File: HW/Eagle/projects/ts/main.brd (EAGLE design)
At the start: 80 x 45 mm, 47 parts, among them IC1 4050D, Q1 20 MHz, T1 IRFZ24N, T2 IRFZ24N, U1 ATMEGA328P-PU, U2 LM2576T, U3 HT7533, U4 LM75

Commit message: Replaced R1 due to improper LCD reset procedure
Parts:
- R1: value 10k -> 1M
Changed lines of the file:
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@@
 <attribute name="VALUE" x="42.21" y="16.27" size="1.27" layer="27" rot="R270"/>
 </element>
-<element name="R1" library="rcl" package="R0805" value="10k" x="58.5" y="41.5" smashed="yes">
+<element name="R1" library="rcl" package="R0805" value="1M" x="58.5" y="41.5" smashed="yes">
 <attribute name="NAME" x="60.865" y="41.27" size="1.27" layer="25"/>
 <attribute name="VALUE" x="57.865" y="38.96" size="1.27" layer="27"/>

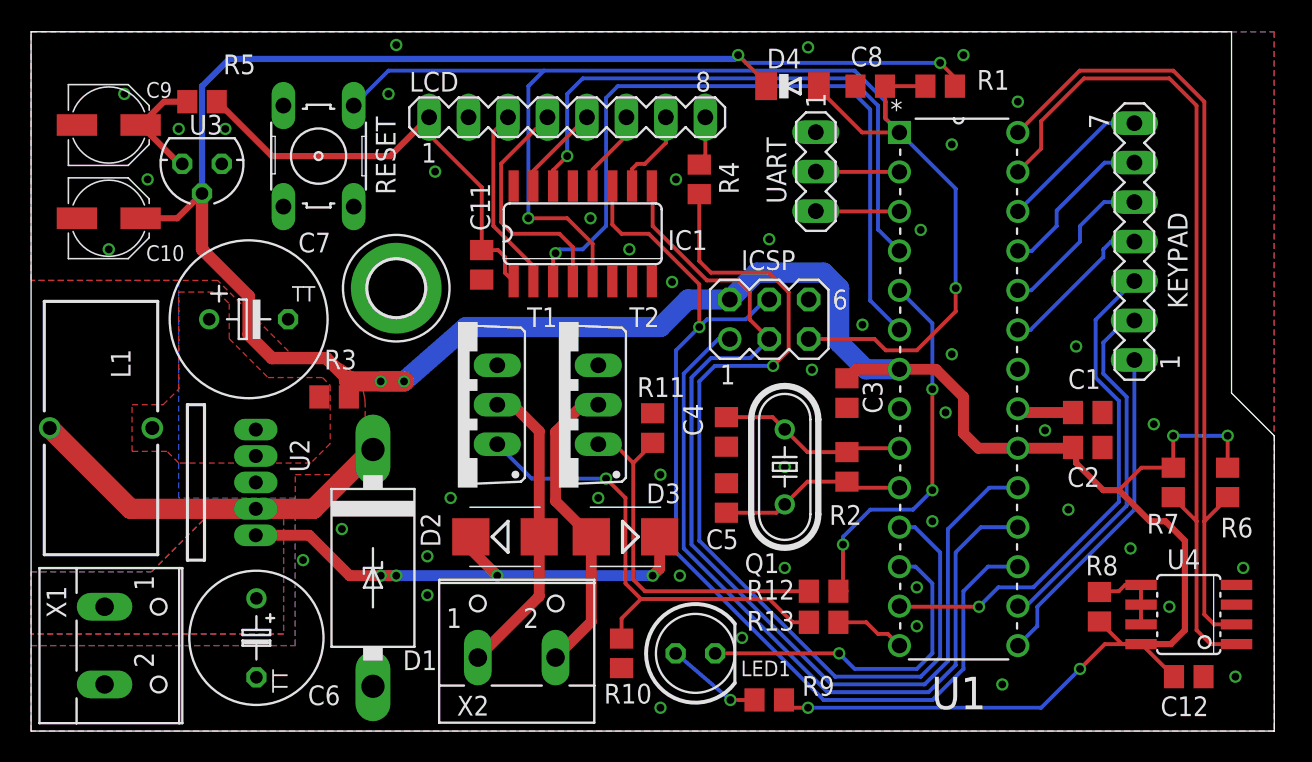
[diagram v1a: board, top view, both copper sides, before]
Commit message: [HW] Updated PCB
Fixed keypad connection. Removed copper from underneath the temperature
sensor. Made temperature sensor removable.
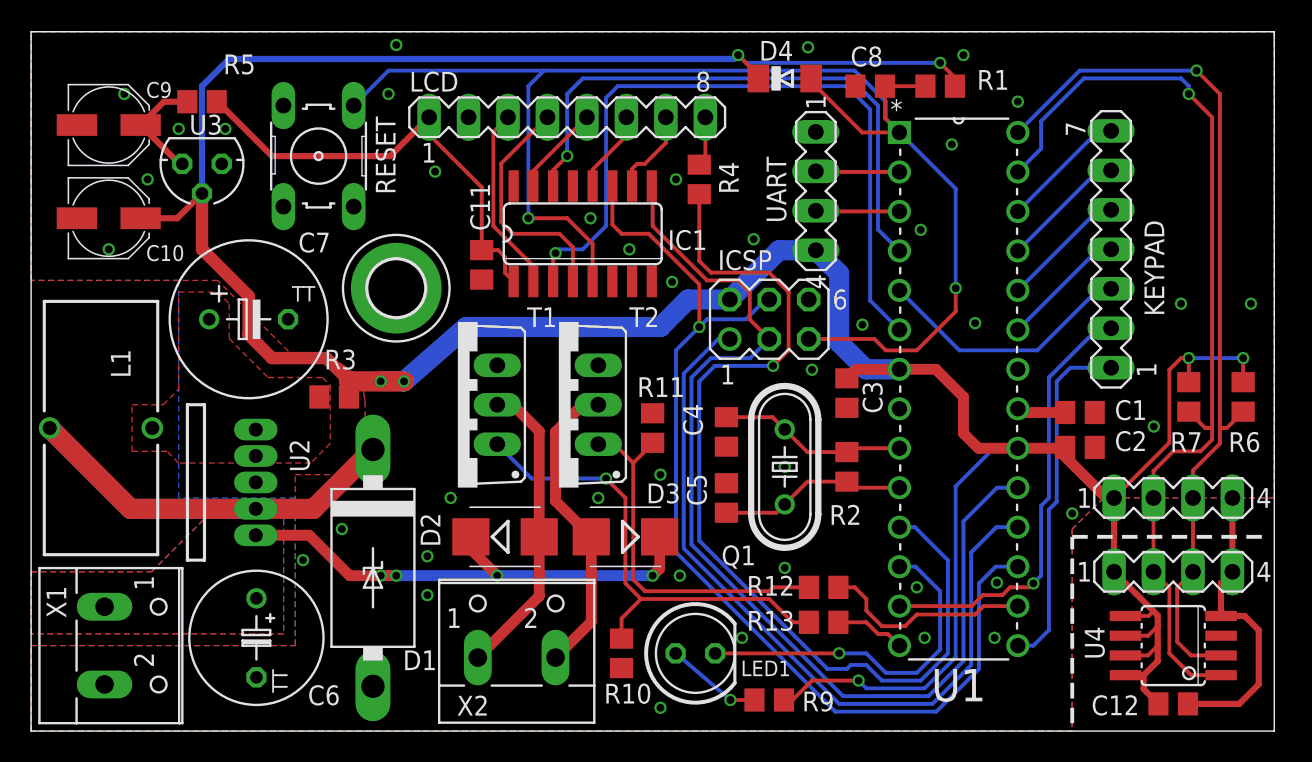
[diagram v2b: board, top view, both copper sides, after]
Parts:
- removed R8: 4.7k, rcl:R0805
- added TEMP_A, TEMP_B: (no value), con-lstb:MA04-1
- UART: device con-lstb:MA03-1 -> con-lstb:MA04-1
- moved R6 5.59 mm to (78.0, 21.5)
- moved R7 5.59 mm to (74.5, 21.5)
- moved U4 2.24 mm to (73.5, 5.50)
- moved C12 2.02 mm to (73.5, 1.75)
- moved KEYPAD 1.58 mm to (69.5, 31.0)
- moved UART 1.25 mm to (50.5, 34.8)
- moved D4 0.71 mm to (48.5, 42.0)
- moved C1 0.50 mm to (67.5, 20.5)
- moved C2 0.50 mm to (67.5, 18.2)
- moved R12 0.25 mm to (51.0, 9.25)
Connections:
- removed net N$5: R8.1, U4.5, U4.6, U4.7
- net GND: now also TEMP_A.4, TEMP_B.4
- net KEYPAD_C1: now also U1.13; no longer U1.16
- net KEYPAD_C2: now also U1.5; no longer U1.13
- net OUT2: now also U1.16; no longer U1.5
- net SCL: now also TEMP_A.3, TEMP_B.3
- net SDA: now also TEMP_A.2, TEMP_B.2
- net VCC: now also TEMP_A.1, TEMP_B.1, U4.5, U4.6, U4.7, UART.4; no longer R8.2
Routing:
- net GND: track 0.00 -> 19.3 mm, vias 46 -> 41
- net KEYPAD_C2: track 32.8 -> 16.9 mm, vias 1 -> 0
- net N$7: track 24.5 -> 40.0 mm
- net VCC: track 209.1 -> 222.6 mm, vias 8 -> 7
- net OUT2: track 24.8 -> 13.6 mm, vias 3 -> 0
- net SDA: track 54.6 -> 60.7 mm, vias 0 -> 1
- net N$5: track 5.41 -> 0.00 mm
- net SCL: track 52.0 -> 57.0 mm, vias 0 -> 1
- net KEYPAD_C1: track 23.4 -> 28.2 mm, vias 0 -> 1
- net KEYPAD_R2: track 10.4 -> 8.15 mm
- net KEYPAD_R1: track 10.4 -> 8.15 mm
- net KEYPAD_R0: track 10.1 -> 8.15 mm
- net KEYPAD_R3: track 9.85 -> 8.15 mm
- net KEYPAD_C0: track 21.5 -> 22.5 mm
- net LCD_LED_5V: track 61.1 -> 62.1 mm
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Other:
- outline, holes or cut-outs redrawn

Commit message: [HW] LCD chip select
Using NSS microcontroller output to drive LCD chip select.
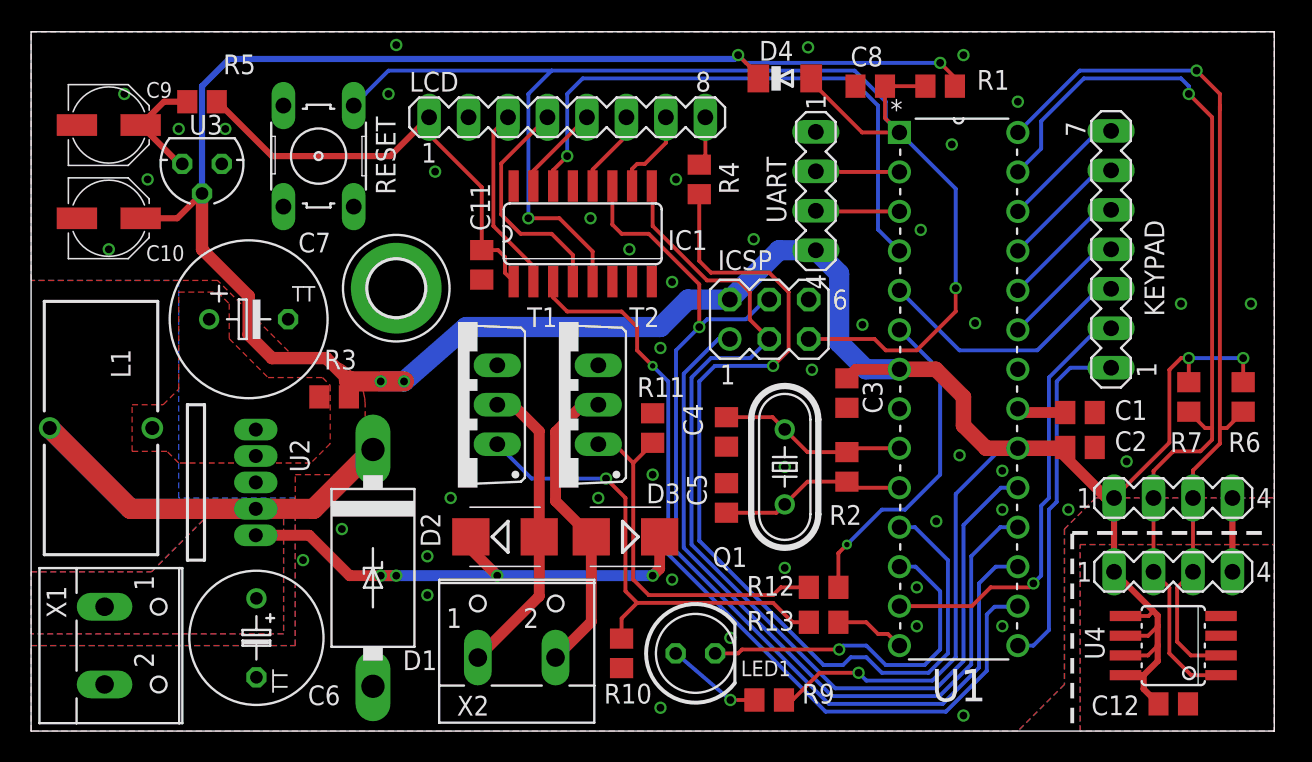
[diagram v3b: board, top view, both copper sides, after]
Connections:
- net LCD_SCE_5V: now also U1.16; no longer U1.6
- net OUT2: now also U1.6; no longer U1.16
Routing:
- net GND: track 19.3 -> 4.75 mm, vias 41 -> 46
- net OUT2: track 13.6 -> 21.2 mm, vias 0 -> 1
- net LCD_SCE_5V: track 47.0 -> 54.3 mm
- net MISO: track 49.7 -> 49.1 mm
- net VCC: track 222.6 -> 222.1 mm
- net LCD_RST: track 15.5 -> 14.9 mm
- net SCK: track 66.8 -> 66.2 mm
- net MOSI: track 66.8 -> 66.3 mm
- added copper zone on layer 16, net N$2

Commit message: [HW] Minor modifications
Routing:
- net NRST: track 92.4 -> 94.6 mm
- net GND: vias 46 -> 47
- removed copper zone on layer 16, net N$2
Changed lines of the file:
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@@
 <wire x1="80" y1="45" x2="80" y2="0" width="0" layer="20"/>
 <wire x1="80" y1="0" x2="0" y2="0" width="0" layer="20"/>
-<wire x1="67" y1="0.5" x2="67" y2="12.75" width="0.25" layer="21" style="dashdot"/>
-<wire x1="67" y1="12.75" x2="79.5" y2="12.75" width="0.25" layer="21" style="dashdot"/>
-<wire x1="67" y1="0.5" x2="67" y2="12.75" width="0.25" layer="22" style="dashdot"/>
-<wire x1="67" y1="12.75" x2="79.5" y2="12.75" width="0.25" layer="22" style="dashdot"/>
+<wire x1="67.25" y1="0.5" x2="67.25" y2="12.5" width="0.25" layer="21" style="dashdot"/>
+<wire x1="67.25" y1="12.5" x2="79.5" y2="12.5" width="0.25" layer="21" style="dashdot"/>
+<wire x1="67.25" y1="0.5" x2="67.25" y2="12.5" width="0.25" layer="22" style="dashdot"/>
+<wire x1="67.25" y1="12.5" x2="79.5" y2="12.5" width="0.25" layer="22" style="dashdot"/>
 </plain>
 <attributes>
@@
 <via x="41.25" y="28.9" extent="1-16" drill="0.5"/>
 <via x="46.5" y="31.65" extent="1-16" drill="0.5"/>
-<via x="53.5" y="26.15" extent="1-16" drill="0.5"/>
+<via x="53.5" y="27.4" extent="1-16" drill="0.5"/>
 <via x="57.25" y="32.25" extent="1-16" drill="0.5"/>
 <via x="41.25" y="9.75" extent="1-16" drill="0.5"/>
@@
 <via x="62.5" y="14.25" extent="1-16" drill="0.5"/>
 <via x="66.75" y="14.25" extent="1-16" drill="0.5"/>
-<polygon width="0.25" layer="1">
-<vertex x="67.5" y="12"/>
-<vertex x="80" y="12"/>
-<vertex x="80" y="0"/>
-<vertex x="67.5" y="0"/>
-</polygon>
 <via x="59.75" y="17.75" extent="1-16" drill="0.5"/>
 <via x="62.5" y="16.75" extent="1-16" drill="0.5"/>
+<via x="53.5" y="25.65" extent="1-16" drill="0.5"/>
+<polygon width="0.25" layer="1">
+<vertex x="76.5" y="12"/>
+<vertex x="78.25" y="12"/>
+<vertex x="78.75" y="11.5"/>
+<vertex x="78.75" y="2.25"/>
+<vertex x="77" y="0.5"/>
+<vertex x="74.5" y="0.5"/>
+<vertex x="73.5" y="1.5"/>
+<vertex x="73.5" y="3"/>
+<vertex x="76" y="5.5"/>
+<vertex x="76" y="11.5"/>
+</polygon>
 </signal>
 <signal name="VCC">
@@
 <wire x1="50.7" y1="41.3" x2="50.2" y2="42" width="0.25" layer="1"/>
 <wire x1="55.88" y1="38.52" x2="53.48" y2="38.52" width="0.25" layer="1"/>
-<wire x1="50.04" y1="25.23" x2="54.27" y2="25.23" width="0.25" layer="1"/>
-<wire x1="54.27" y1="25.23" x2="55" y2="24.5" width="0.25" layer="1"/>
-<wire x1="55" y1="24.5" x2="57" y2="24.5" width="0.25" layer="1"/>
+<wire x1="55" y1="24.5" x2="54.52" y2="24.98" width="0.25" layer="1"/>
+<wire x1="55" y1="24.5" x2="58" y2="24.5" width="0.25" layer="1"/>
 <via x="59.5" y="28.5" extent="1-16" drill="0.5"/>
 <wire x1="59.5" y1="28.5" x2="59.5" y2="34.9" width="0.25" layer="16"/>
@@
 <wire x1="32" y1="33" x2="32" y2="41" width="0.25" layer="16"/>
 <wire x1="32" y1="41" x2="33.5" y2="42.5" width="0.25" layer="16"/>
-<wire x1="57" y1="24.5" x2="59.5" y2="27" width="0.25" layer="1"/>
-<wire x1="59.5" y1="27" x2="59.5" y2="28.5" width="0.25" layer="1"/>
+<wire x1="58" y1="24.5" x2="59.5" y2="26" width="0.25" layer="1"/>
+<wire x1="59.5" y1="26" x2="59.5" y2="28.5" width="0.25" layer="1"/>
 <wire x1="53.48" y1="38.52" x2="50.7" y2="41.3" width="0.25" layer="1"/>
+<wire x1="54.52" y1="24.98" x2="54.52" y2="25.98" width="0.25" layer="1"/>
+<wire x1="54.52" y1="25.98" x2="54" y2="26.5" width="0.25" layer="1"/>
+<wire x1="54" y1="26.5" x2="51.31" y2="26.5" width="0.25" layer="1"/>
+<wire x1="51.31" y1="26.5" x2="50.04" y2="25.23" width="0.25" layer="1"/>
 </signal>
 <signal name="N$7">
@@
 <vertex x="9.5" y="17.25"/>
 <vertex x="8.75" y="18"/>
-<vertex x="6.5" y="18"/>
-<vertex x="6.5" y="21"/>
+<vertex x="7.25" y="18"/>
+<vertex x="6.5" y="18.75"/>
+<vertex x="6.5" y="20.25"/>
+<vertex x="7.25" y="21"/>
 <vertex x="8.5" y="21"/>
 <vertex x="9.5" y="22"/>
@@
 <wire x1="48.25" y1="9.25" x2="50.05" y2="9.25" width="0.25" layer="1"/>
 </signal>
-<signal name="N$2">
-<polygon width="0.25" layer="16">
-<vertex x="67.5" y="12"/>
-<vertex x="80" y="12"/>
-<vertex x="80" y="0"/>
-<vertex x="67.5" y="0"/>
-</polygon>
-</signal>
 </signals>

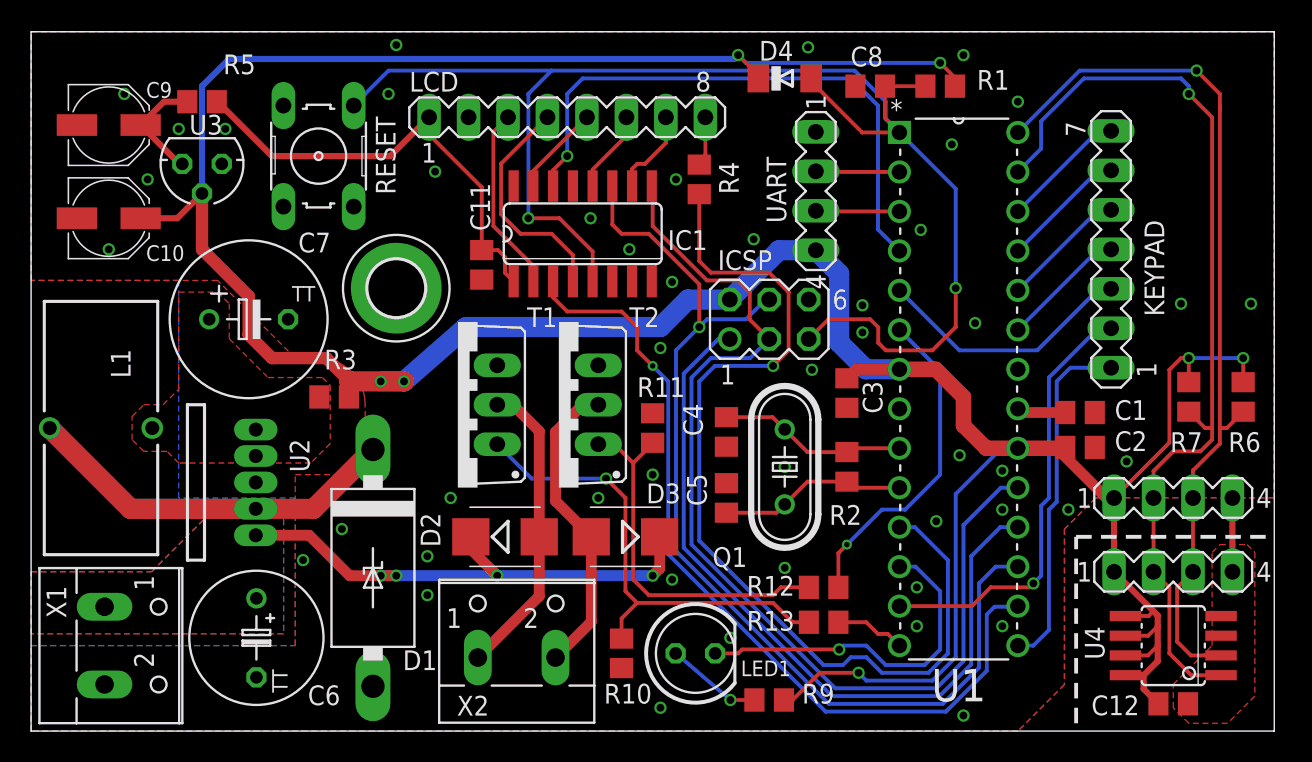
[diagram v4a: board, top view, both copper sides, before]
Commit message: [HW] Removed some parts, updated layout
Removed unessential parts (0 Ohm resistor, reset pin protection diode).
Optimized layout to optimize some connections.
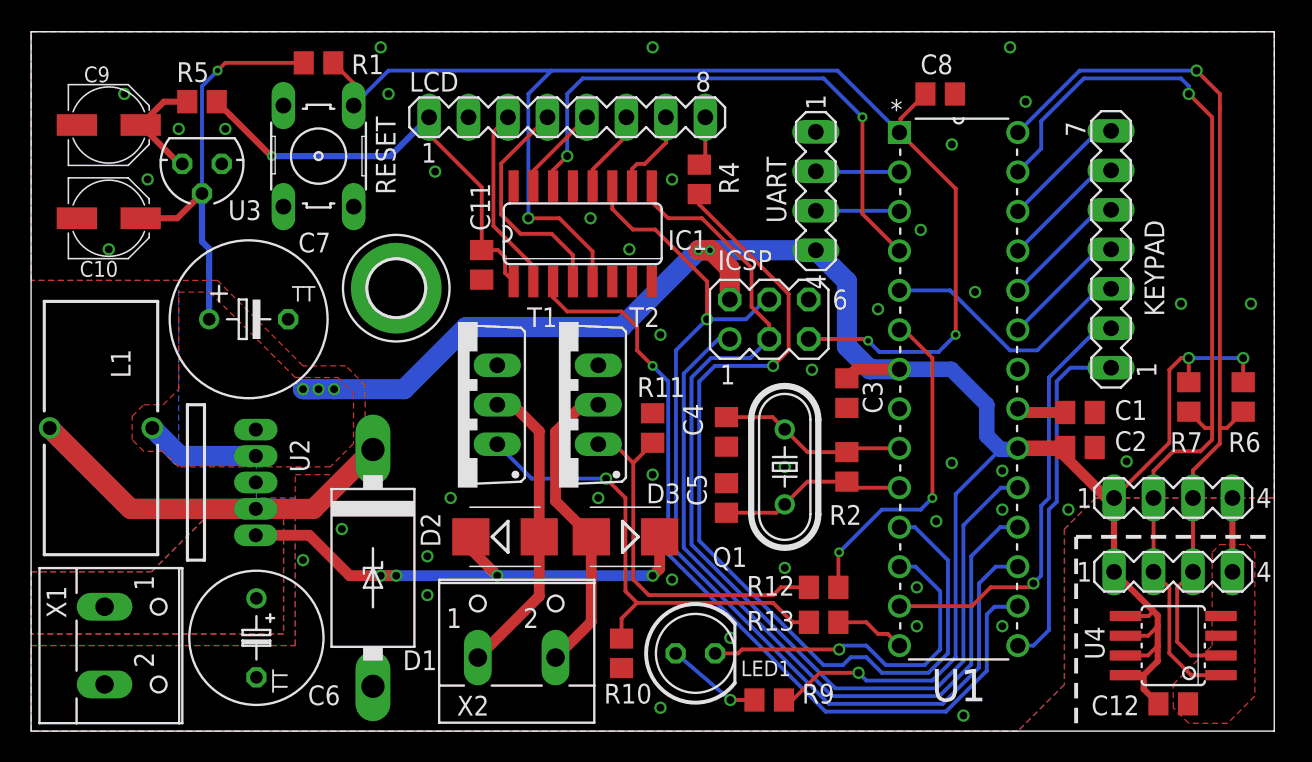
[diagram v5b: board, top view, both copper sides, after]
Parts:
- removed D4: (no value), diode:MINIMELF
- removed R3: 0R, rcl:R0805
- moved R1 40.0 mm to (18.5, 43.0), turned to 180 degrees
- moved C8 4.53 mm to (58.5, 41.0), turned to 180 degrees
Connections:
- net N$10 renamed OUT1_OC
- net N$11 renamed OUT2_OC
- net N$7 renamed OUT_5V
- removed net N$8: C7.+, L1.1, R3.1, U2.4
- net NRST: no longer D4.A
- net VCC: now also C7.+, L1.1, U2.4; no longer D4.C, R3.2
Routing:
- net VCC: track 222.1 -> 178.8 mm, vias 7 -> 9
- net NRST: track 94.6 -> 86.1 mm, vias 2 -> 3
- net LCD_LED_5V: track 61.9 -> 59.7 mm
- net LCD_DC_5V: track 37.4 -> 36.3 mm, vias 1 -> 2
- net +3V3: track 29.3 -> 29.6 mm, vias 0 -> 1
- net OUT2: track 21.2 -> 21.6 mm, vias 1 -> 2
- net GND: vias 47 -> 44
- added copper zone on layer 1, net VCC
- removed copper zone on layer 1, net N$8
